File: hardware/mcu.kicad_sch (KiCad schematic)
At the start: 33 parts, among them J3 SW, SW1 BTN_ACT, SW2 BTN_DEACT, U1 STM32F103C8T6, Y1 32KHz, Y2 8MHz

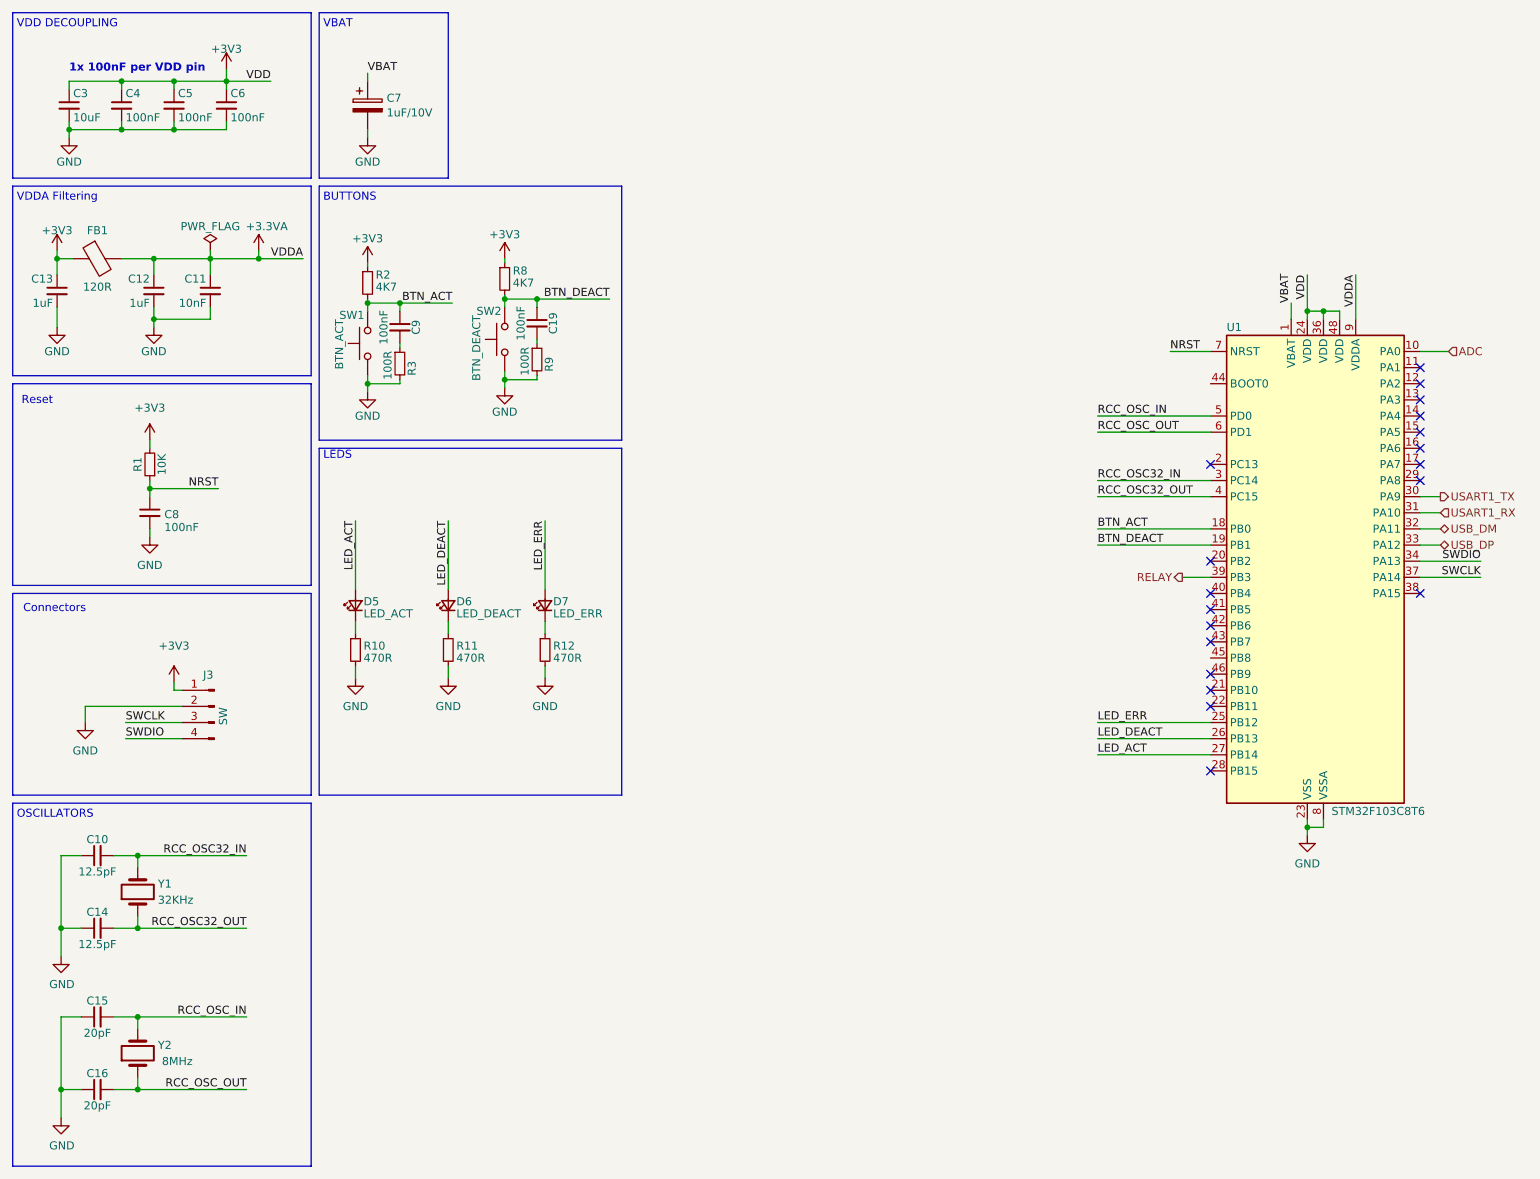
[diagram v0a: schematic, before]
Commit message: MCU BOOT0 mistake fixed
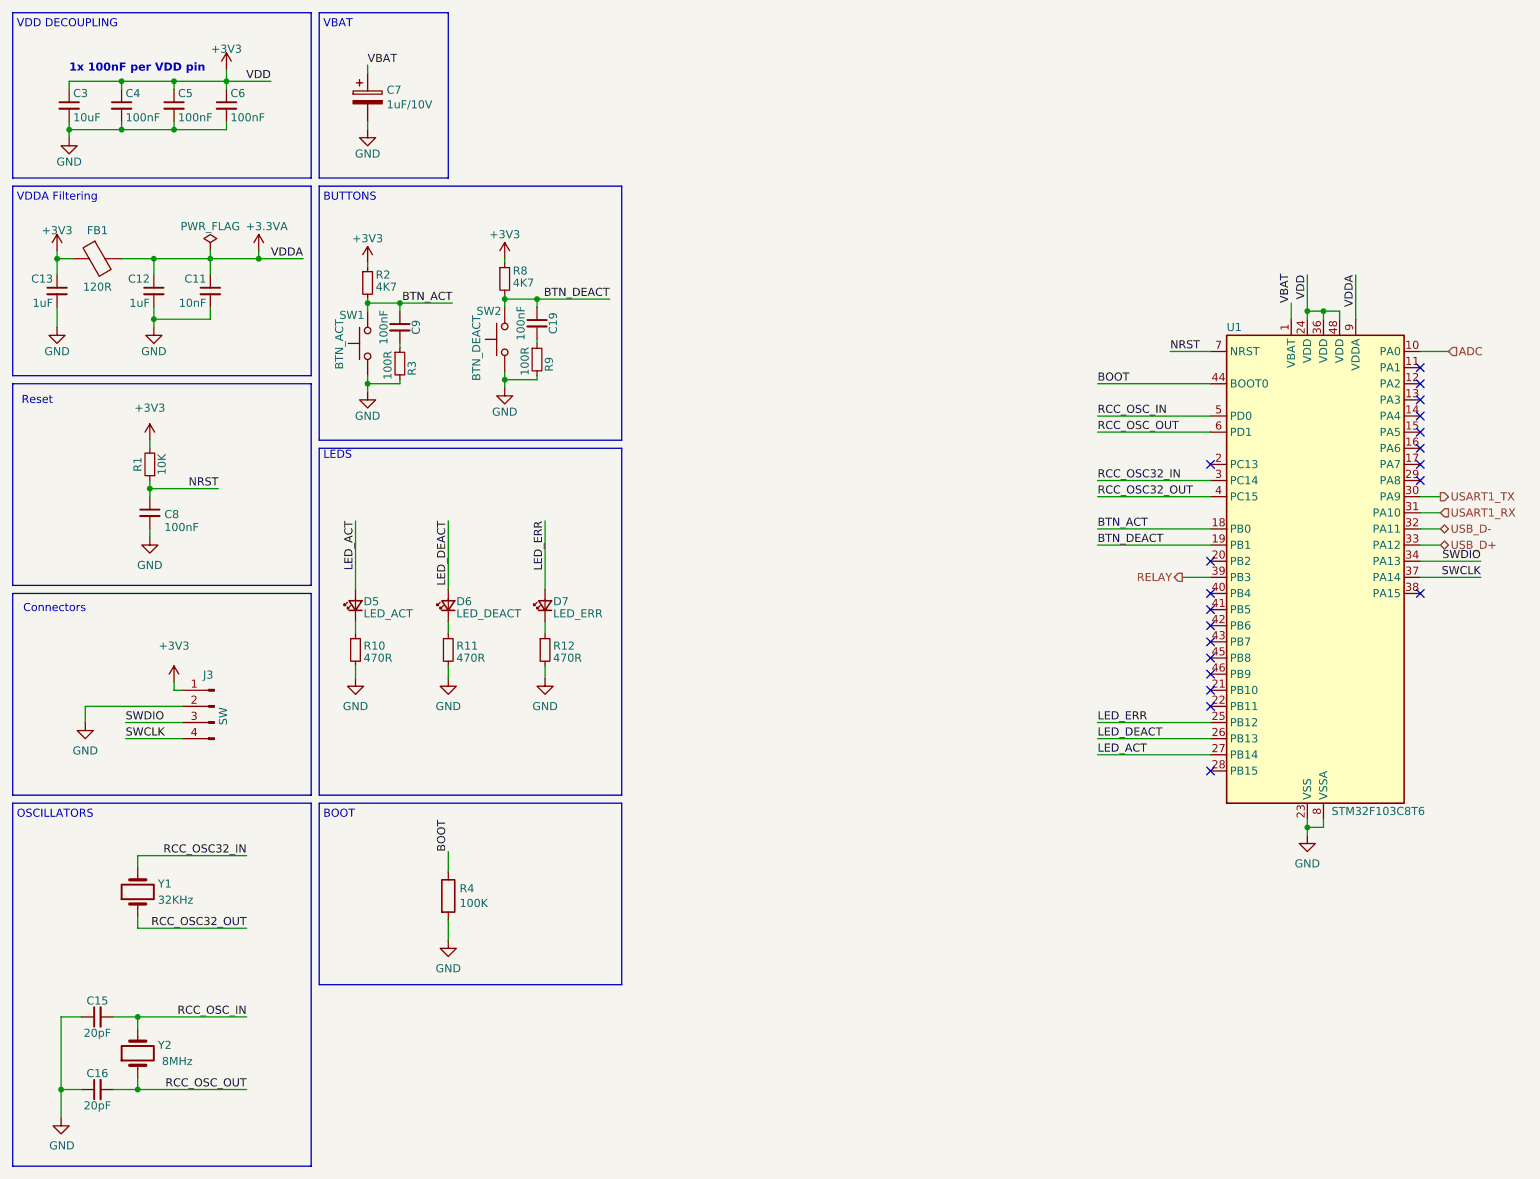
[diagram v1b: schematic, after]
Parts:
- removed C10, C14: 12.5pF, Capacitor_SMD:C_0603_1608Metric, symbol Device:C_Small
- added R4: 100K, Resistor_SMD:R_0603_1608Metric, symbol Device:R
- C11: DigikeyPN (none) -> 13-CC0100KRX5R4BB103TR-ND
- C12, C13: DigikeyPN (none) -> 311-1447-6-ND
- C15, C16: DigikeyPN (none) -> 399-C0603C200G8HAC7867DKR-ND
- C3: DigikeyPN (none) -> 13-CC0603MPX5R5BB106DKR-ND
- C4, C5, C6: DigikeyPN (none) -> AC0603KPX7R7BB104
- C7: Digikey 478-12231-6-ND -> (none); DigikeyPN (none) -> 478-12231-6-ND
- D5: DigikeyPN (none) -> 1830-1004-ND
- D6: DigikeyPN (none) -> 1830-1001-ND
- D7: DigikeyPN (none) -> 1830-1000-ND
- FB1: DigikeyPN (none) -> 732-4665-6-ND
- J3: now left out of the parts list
- R1: DigikeyPN (none) -> RNCP0603FTD10K0DKR-ND
- R10, R11, R12: DigikeyPN (none) -> 1292-WR06X471JTLDKR-ND
- R2, R8: DigikeyPN (none) -> 13-RC1206FR-134K7LDKR-ND
- R3, R9: DigikeyPN (none) -> RR08P100DDKR-ND
- SW1, SW2: DigikeyPN (none) -> 732-13663-6-ND
- U1: DigikeyPN (none) -> 497-6063-ND
- Y2: DigikeyPN X1123-ND -> 631-1010-6-ND
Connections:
- net GND: now also R4.2
- net SWCLK: now also J3.4 (Pin_4); no longer J3.3 (Pin_3)
- net SWDIO: now also J3.3 (Pin_3); no longer J3.4 (Pin_4)
- net BOOT: now reaches U1.44 (BOOT0)
- net BOOT: now also R4.1
- net USB_DM renamed USB_D-
- net USB_DP renamed USB_D+
- no-connect marks 19 -> 20
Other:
- note added: "BOOT"
- moved on the sheet: C7
